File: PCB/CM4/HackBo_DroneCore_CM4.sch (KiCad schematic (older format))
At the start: 0 parts

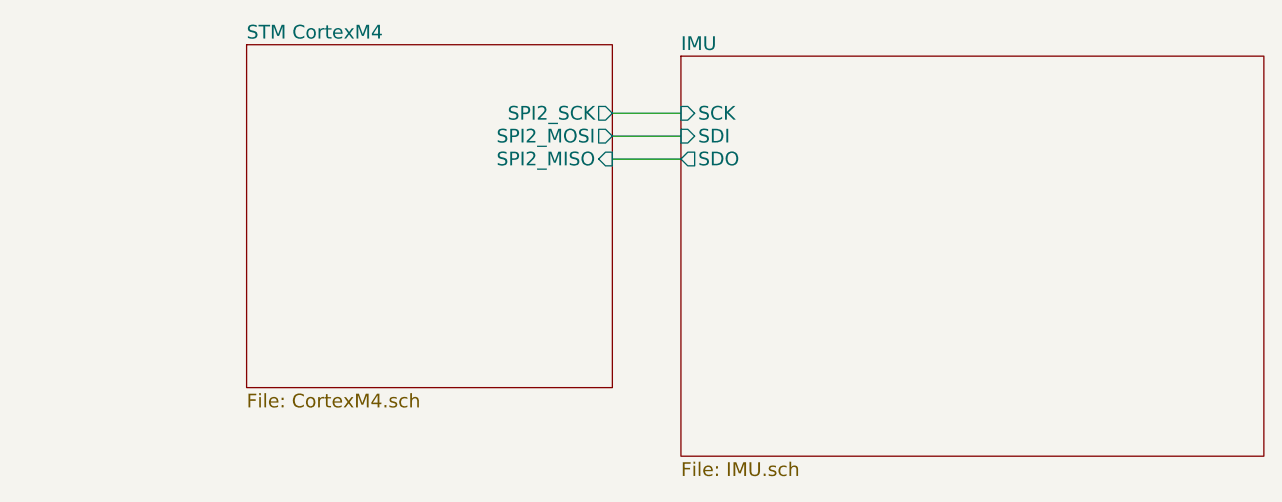
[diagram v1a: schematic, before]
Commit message: Compass connected
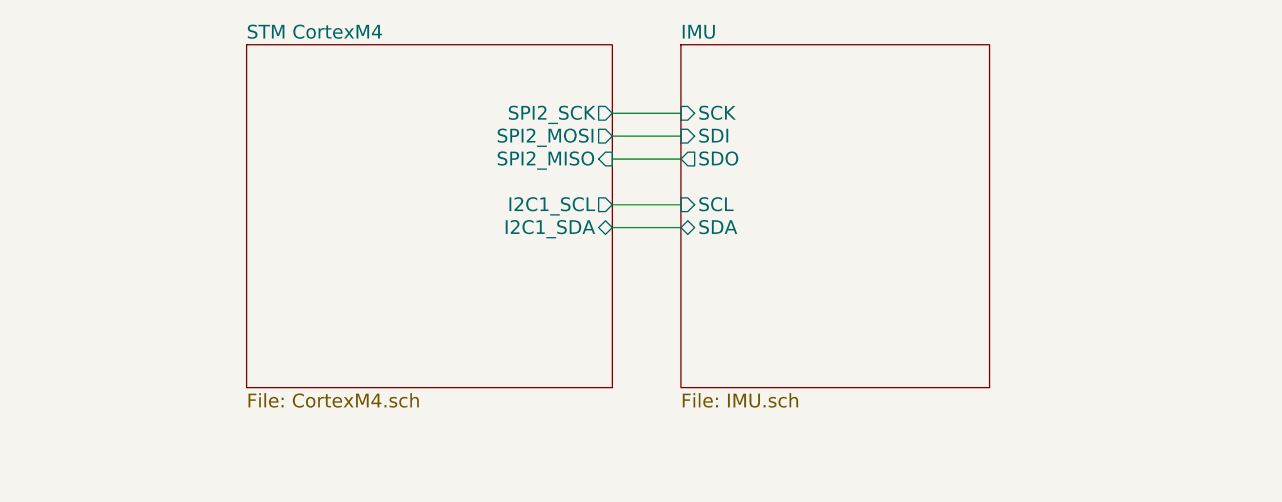
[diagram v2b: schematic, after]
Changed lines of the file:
@@
-EESchema Schematic File Version 2  date Sat 03 Nov 2012 10:35:30 PM COT
+EESchema Schematic File Version 2  date Sat 03 Nov 2012 10:53:34 PM COT
 LIBS:power
 LIBS:device
@@
 $EndDescr
 $Sheet
-S 5300 2400 2550 1750
+S 5300 2350 1350 1500
 U 50940AA1
 F0 "IMU" 60
@@
 F3 "SCK" I L 5300 2650 60
 F4 "SDO" O L 5300 2850 60
+F5 "SDA" B L 5300 3150 60
+F6 "SCL" I L 5300 3050 60
 $EndSheet
 $Sheet
@@
 F3 "SPI2_MISO" I R 5000 2850 60
 F4 "SPI2_SCK" O R 5000 2650 60
+F5 "I2C1_SCL" O R 5000 3050 60
+F6 "I2C1_SDA" B R 5000 3150 60
 $EndSheet
 Wire Wire Line
@@
 Wire Wire Line
 	5000 2850 5300 2850
+Wire Wire Line
+	5000 3050 5300 3050
+Wire Wire Line
+	5000 3150 5300 3150
 $EndSCHEMATC

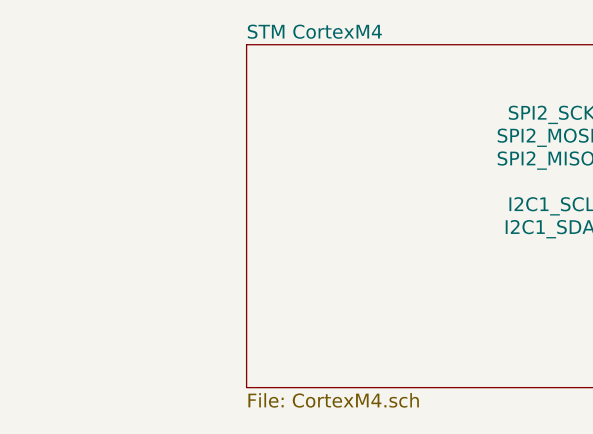
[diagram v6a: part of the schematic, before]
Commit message: Connection to pwm connectors.
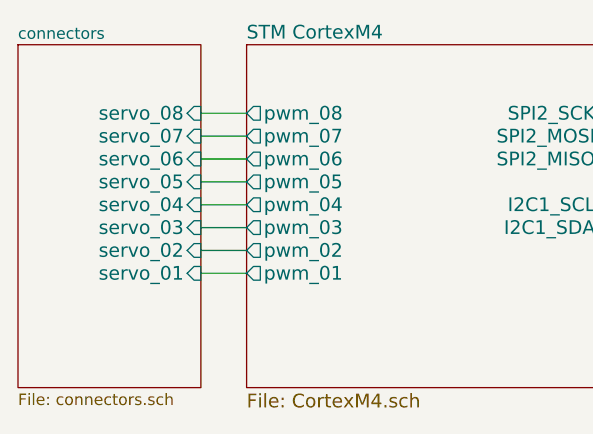
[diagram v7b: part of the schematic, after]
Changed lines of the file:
@@
-EESchema Schematic File Version 2  date Mon 05 Nov 2012 06:52:04 AM COT
+EESchema Schematic File Version 2  date Mon 05 Nov 2012 10:11:56 PM EST
 LIBS:power
 LIBS:device
@@
 LIBS:bmp085
 LIBS:mpu6000
+LIBS:ap1115a
 LIBS:HackBo_DroneCore_CM4-cache
 EELAYER 27 0
@@
 $Descr A4 11693 8268
 encoding utf-8
-Sheet 1 3
+Sheet 1 4
 Title ""
-Date "5 nov 2012"
+Date "6 nov 2012"
 Rev ""
 Comp ""
@@
 F5 "I2C1_SCL" O R 5000 3050 60
 F6 "I2C1_SDA" B R 5000 3150 60
+F7 "pwm_01" O L 3400 3350 60
+F8 "pwm_02" O L 3400 3250 60
+F9 "pwm_03" O L 3400 3150 60
+F10 "pwm_04" O L 3400 3050 60
+F11 "pwm_05" O L 3400 2950 60
+F12 "pwm_06" O L 3400 2850 60
+F13 "pwm_07" O L 3400 2750 60
+F14 "pwm_08" O L 3400 2650 60
 $EndSheet
 Wire Wire Line
@@
 Wire Wire Line
 	5000 3150 5300 3150
+$Sheet
+S 2400 2350 800  1500
+U 50987FB7
+F0 "connectors" 50
+F1 "connectors.sch" 50
+F2 "servo_08" I R 3200 2650 60
+F3 "servo_07" I R 3200 2750 60
+F4 "servo_06" I R 3200 2850 60
+F5 "servo_05" I R 3200 2950 60
+F6 "servo_04" I R 3200 3050 60
+F7 "servo_03" I R 3200 3150 60
+F8 "servo_02" I R 3200 3250 60
+F9 "servo_01" I R 3200 3350 60
+$EndSheet
+Wire Wire Line
+	3200 2650 3400 2650
+Wire Wire Line
+	3400 2750 3200 2750
+Wire Wire Line
+	3200 2850 3400 2850
+Wire Wire Line
+	3400 2950 3200 2950
+Wire Wire Line
+	3200 3050 3400 3050
+Wire Wire Line
+	3400 3150 3200 3150
+Wire Wire Line
+	3200 3250 3400 3250
+Wire Wire Line
+	3400 3350 3200 3350
 $EndSCHEMATC

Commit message: 5v power  and reset
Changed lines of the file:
@@
-EESchema Schematic File Version 2  date Mon 05 Nov 2012 10:11:56 PM EST
+EESchema Schematic File Version 2  date Tue 06 Nov 2012 07:35:26 PM EST
 LIBS:power
 LIBS:device
@@
 Sheet 1 4
 Title ""
-Date "6 nov 2012"
+Date "7 nov 2012"
 Rev ""
 Comp ""
@@
 F13 "pwm_07" O L 3400 2750 60
 F14 "pwm_08" O L 3400 2650 60
+F15 "RESET" I L 3400 3650 60
 $EndSheet
 Wire Wire Line
@@
 F8 "servo_02" I R 3200 3250 60
 F9 "servo_01" I R 3200 3350 60
+F10 "RESET" O R 3200 3650 60
 $EndSheet
 Wire Wire Line
@@
 Wire Wire Line
 	3400 3350 3200 3350
+Wire Wire Line
+	3200 3650 3400 3650
 $EndSCHEMATC
